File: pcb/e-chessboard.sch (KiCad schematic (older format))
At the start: 66 parts, among them J1 POWER, J2 UART, Q1 BC847, Q2 BC847, SW1 Reset, SW2 Boot, U1 ESP32-WROOM-32U, U10 MAGNET_LDR, U11 MAGNET_LDR, U12 MAGNET_LDR, U13 NCV7608, U2 AOZ1280, U3 NCV7608, U4 MAGNET_LDR, U5 MAGNET_LDR, U6 MAGNET_LDR, U7 MAGNET_LDR, U8 MAGNET_LDR, U9 MAGNET_LDR

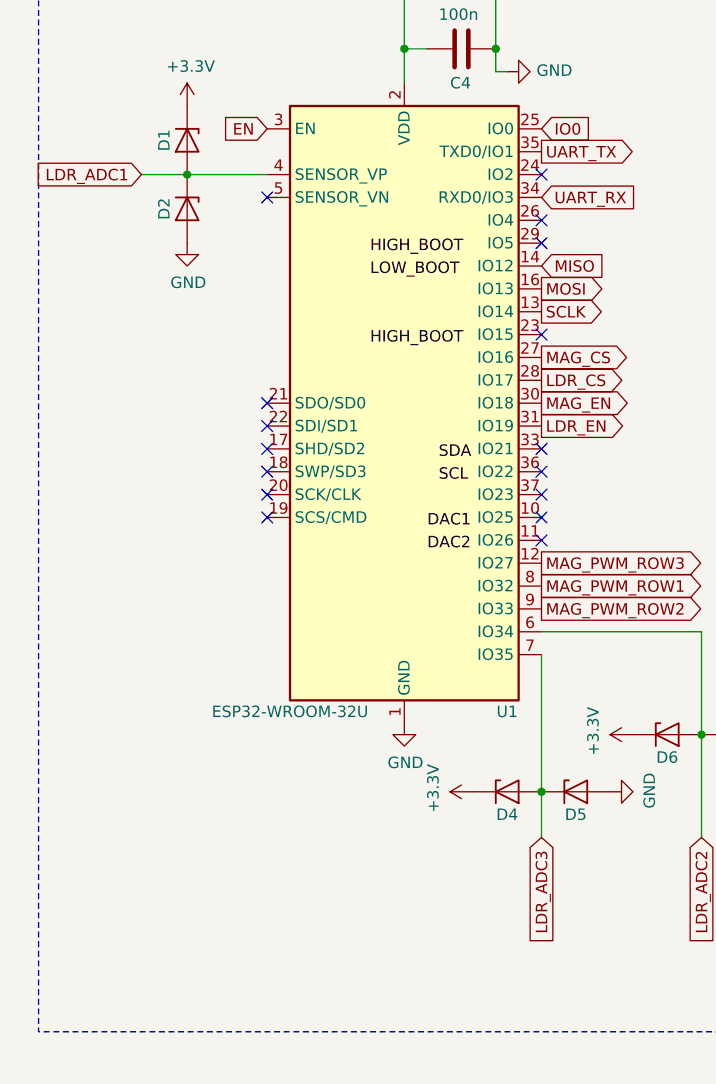
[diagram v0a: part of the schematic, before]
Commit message: fix(kicad): redesign pcb
Redesigning the pcb with the new ldr matrix.
I'm pretty sure, that's it's still not working, but for the first
prototype I will put the focus on the magnets and not the ldr. Just a
prove a concept.
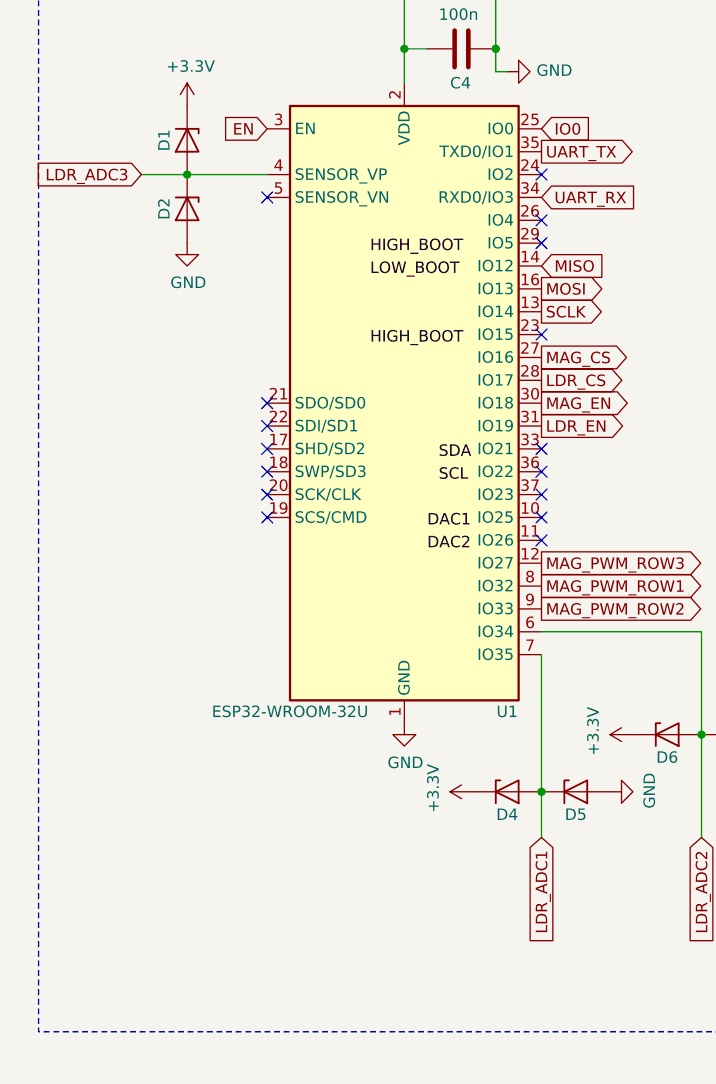
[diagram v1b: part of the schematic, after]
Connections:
- net LDR_ADC1: now also D4.2 (A), D5.1 (K), U1.7 (IO35); no longer D1.2 (A), D2.1 (K), U1.4 (SENSOR_VP)
- net LDR_ADC3: now also D1.2 (A), D2.1 (K), U1.4 (SENSOR_VP); no longer D4.2 (A), D5.1 (K), U1.7 (IO35)
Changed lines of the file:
@@
 MAG_COL_3
 $Comp
-L power:GND #PWR025
+L power:GND #PWR026
 U 1 1 5E693B2A
 P 8750 2700
-F 0 "#PWR025" H 8750 2450 50  0001 C CNN
+F 0 "#PWR026" H 8750 2450 50  0001 C CNN
 F 1 "GND" V 8755 2572 50  0000 R CNN
 F 2 "" H 8750 2700 50  0001 C CNN
@@
 Connection ~ 8750 2700
 $Comp
-L power:GND #PWR030
+L power:GND #PWR031
 U 1 1 5E693B35
 P 9600 2750
-F 0 "#PWR030" H 9600 2500 50  0001 C CNN
+F 0 "#PWR031" H 9600 2500 50  0001 C CNN
 F 1 "GND" V 9605 2622 50  0000 R CNN
 F 2 "" H 9600 2750 50  0001 C CNN
@@
 NoConn ~ 9600 2050
 $Comp
-L power:+12V #PWR027
+L power:+12V #PWR028
 U 1 1 5E693B3E
 P 8850 1850
-F 0 "#PWR027" H 8850 1700 50  0001 C CNN
+F 0 "#PWR028" H 8850 1700 50  0001 C CNN
 F 1 "+12V" V 8865 1978 50  0000 L CNN
 F 2 "" H 8850 1850 50  0001 C CNN
@@
 $EndComp
 $Comp
-L power:+12V #PWR026
+L power:+12V #PWR027
 U 1 1 5E693B44
 P 8850 1550
-F 0 "#PWR026" H 8850 1400 50  0001 C CNN
+F 0 "#PWR027" H 8850 1400 50  0001 C CNN
 F 1 "+12V" V 8865 1678 50  0000 L CNN
 F 2 "" H 8850 1550 50  0001 C CNN
@@
 $EndComp
 $Comp
-L power:+12V #PWR029
+L power:+12V #PWR030
 U 1 1 5E693B4A
 P 9600 1550
-F 0 "#PWR029" H 9600 1400 50  0001 C CNN
+F 0 "#PWR030" H 9600 1400 50  0001 C CNN
 F 1 "+12V" V 9615 1678 50  0000 L CNN
 F 2 "" H 9600 1550 50  0001 C CNN
@@
 NoConn ~ 9600 1850
 $Comp
-L power:GND #PWR028
+L power:GND #PWR029
 U 1 1 5E6A7D5E
 P 8850 2450
-F 0 "#PWR028" H 8850 2200 50  0001 C CNN
+F 0 "#PWR029" H 8850 2200 50  0001 C CNN
 F 1 "GND" V 8855 2322 50  0000 R CNN
 F 2 "" H 8850 2450 50  0001 C CNN
@@
 $EndComp
 $Comp
-L power:+12V #PWR032
+L power:+12V #PWR033
 U 1 1 5E6A7F72
 P 10150 1950
-F 0 "#PWR032" H 10150 1800 50  0001 C CNN
+F 0 "#PWR033" H 10150 1800 50  0001 C CNN
 F 1 "+12V" V 10165 2078 50  0000 L CNN
 F 2 "" H 10150 1950 50  0001 C CNN
@@
 $EndComp
 $Comp
-L power:GND #PWR031
+L power:GND #PWR032
 U 1 1 5E6A8CA5
 P 10150 1650
-F 0 "#PWR031" H 10150 1400 50  0001 C CNN
+F 0 "#PWR032" H 10150 1400 50  0001 C CNN
 F 1 "GND" H 10155 1477 50  0000 C CNN
 F 2 "" H 10150 1650 50  0001 C CNN
@@
 $EndComp
 $Comp
-L power:+3.3V #PWR023
+L power:+3.3V #PWR024
 U 1 1 5E69F100
 P 8300 2250
-F 0 "#PWR023" H 8300 2100 50  0001 C CNN
+F 0 "#PWR024" H 8300 2100 50  0001 C CNN
 F 1 "+3.3V" V 8315 2378 50  0000 L CNN
 F 2 "" H 8300 2250 50  0001 C CNN
@@
 Connection ~ 6500 6750
 $Comp
-L power:+3.3V #PWR016
+L power:+3.3V #PWR017
 U 1 1 5E89D658
 P 6500 6350
-F 0 "#PWR016" H 6500 6200 50  0001 C CNN
+F 0 "#PWR017" H 6500 6200 50  0001 C CNN
 F 1 "+3.3V" H 6550 6350 50  0000 L CNN
 F 2 "" H 6500 6350 50  0001 C CNN
@@
 $EndComp
 $Comp
-L power:GND #PWR017
+L power:GND #PWR018
 U 1 1 5E89DCA1
 P 6500 7050
-F 0 "#PWR017" H 6500 6800 50  0001 C CNN
+F 0 "#PWR018" H 6500 6800 50  0001 C CNN
 F 1 "GND" H 6650 7050 50  0000 R CNN
 F 2 "" H 6500 7050 50  0001 C CNN
@@
 $EndComp
 $Comp
-L power:+3.3V #PWR018
+L power:+3.3V #PWR019
 U 1 1 5E8B01DC
 P 6500 7550
-F 0 "#PWR018" H 6500 7400 50  0001 C CNN
+F 0 "#PWR019" H 6500 7400 50  0001 C CNN
 F 1 "+3.3V" H 6550 7600 50  0000 L CNN
 F 2 "" H 6500 7550 50  0001 C CNN
@@
 	7850 7350 7850 7250
 $Comp
-L power:GND #PWR022
+L power:GND #PWR023
 U 1 1 5E8D6B40
 P 7950 7250
-F 0 "#PWR022" H 7950 7000 50  0001 C CNN
+F 0 "#PWR023" H 7950 7000 50  0001 C CNN
 F 1 "GND" V 8000 7350 50  0000 R CNN
 F 2 "" H 7950 7250 50  0001 C CNN
@@
 $EndComp
 $Comp
-L power:+3.3V #PWR020
+L power:+3.3V #PWR021
 U 1 1 5E8F3DEC
 P 7750 8150
-F 0 "#PWR020" H 7750 8000 50  0001 C CNN
+F 0 "#PWR021" H 7750 8000 50  0001 C CNN
 F 1 "+3.3V" V 7765 8278 50  0000 L CNN
 F 2 "" H 7750 8150 50  0001 C CNN
@@
 $EndComp
 $Comp
-L power:GND #PWR019
+L power:GND #PWR020
 U 1 1 5E8FAC1F
 P 7750 8050
-F 0 "#PWR019" H 7750 7800 50  0001 C CNN
+F 0 "#PWR020" H 7750 7800 50  0001 C CNN
 F 1 "GND" V 7755 7922 50  0000 R CNN
 F 2 "" H 7750 8050 50  0001 C CNN
@@
 EN
 $Comp
-L power:GND #PWR024
+L power:GND #PWR025
 U 1 1 5E6A4B4A
 P 8300 2550
-F 0 "#PWR024" H 8300 2300 50  0001 C CNN
+F 0 "#PWR025" H 8300 2300 50  0001 C CNN
 F 1 "GND" H 8305 2377 50  0000 C CNN
 F 2 "" H 8300 2550 50  0001 C CNN
@@
 	7850 6750 7850 6650
 $Comp
-L power:GND #PWR021
+L power:GND #PWR022
 U 1 1 5EC99E9E
 P 7950 6650
-F 0 "#PWR021" H 7950 6400 50  0001 C CNN
+F 0 "#PWR022" H 7950 6400 50  0001 C CNN
 F 1 "GND" V 8000 6750 50  0000 R CNN
 F 2 "" H 7950 6650 50  0001 C CNN
@@
 MAG_ROW_3
 $Comp
-L power:+12V #PWR041
+L power:+12V #PWR042
 U 1 1 5F4E88F9
 P 14850 2000
-F 0 "#PWR041" H 14850 1850 50  0001 C CNN
+F 0 "#PWR042" H 14850 1850 50  0001 C CNN
 F 1 "+12V" V 14865 2128 50  0000 L CNN
 F 2 "" H 14850 2000 50  0001 C CNN
@@
 $EndComp
 $Comp
-L power:GND #PWR040
+L power:GND #PWR041
 U 1 1 5F4E8905
 P 14850 1700
-F 0 "#PWR040" H 14850 1450 50  0001 C CNN
+F 0 "#PWR041" H 14850 1450 50  0001 C CNN
 F 1 "GND" H 14855 1527 50  0000 C CNN
 F 2 "" H 14850 1700 50  0001 C CNN
@@
 Connection ~ 14850 2000
 $Comp
-L power:GND #PWR038
+L power:GND #PWR039
 U 1 1 5F4F6CE9
 P 13550 2500
-F 0 "#PWR038" H 13550 2250 50  0001 C CNN
+F 0 "#PWR039" H 13550 2250 50  0001 C CNN
 F 1 "GND" V 13555 2372 50  0000 R CNN
 F 2 "" H 13550 2500 50  0001 C CNN
@@
 $EndComp
 $Comp
-L power:+3.3V #PWR034
+L power:+3.3V #PWR035
 U 1 1 5F509788
 P 13000 2300
-F 0 "#PWR034" H 13000 2150 50  0001 C CNN
+F 0 "#PWR035" H 13000 2150 50  0001 C CNN
 F 1 "+3.3V" V 13015 2428 50  0000 L CNN
 F 2 "" H 13000 2300 50  0001 C CNN
@@
 $EndComp
 $Comp
-L power:GND #PWR035
+L power:GND #PWR036
 U 1 1 5F50978E
 P 13000 2600
-F 0 "#PWR035" H 13000 2350 50  0001 C CNN
+F 0 "#PWR036" H 13000 2350 50  0001 C CNN
 F 1 "GND" H 13005 2427 50  0000 C CNN
 F 2 "" H 13000 2600 50  0001 C CNN
@@
 Text GLabel 14300 2500 2    50   Input ~ 0
 LDR_EN
-Text GLabel 1050 4700 0    50   Input ~ 0
+Text GLabel 2800 7600 3    50   Input ~ 0
 LDR_ADC1
 Text GLabel 3500 7600 3    50   Input ~ 0
 LDR_ADC2
-Text GLabel 2800 7600 3    50   Input ~ 0
+Text GLabel 1050 4700 0    50   Input ~ 0
 LDR_ADC3
 $Comp
@@
 MAGNET_LDR_MATRIX
 $Comp
-L power:+3.3V #PWR0101
+L power:+3.3V #PWR016
 U 1 1 5FD145A0
 P 5800 2050
-F 0 "#PWR0101" H 5800 1900 50  0001 C CNN
+F 0 "#PWR016" H 5800 1900 50  0001 C CNN
 F 1 "+3.3V" H 5815 2223 50  0000 C CNN
 F 2 "" H 5800 2050 50  0001 C CNN
@@
 Connection ~ 5800 2050
 $Comp
-L power:PWR_FLAG #FLG0101
+L power:PWR_FLAG #FLG03
 U 1 1 5FD1593F
 P 5800 2050
-F 0 "#FLG0101" H 5800 2125 50  0001 C CNN
+F 0 "#FLG03" H 5800 2125 50  0001 C CNN
 F 1 "PWR_FLAG" V 5800 2178 50  0001 L CNN
 F 2 "" H 5800 2050 50  0001 C CNN
@@
 Wire Wire Line
 	13100 5600 13150 5600
-$Comp
-L Device:D D9
-U 1 1 5EF37B5F
-P 10950 5600
-F 0 "D9" V 10950 5750 50  0000 R CNN
-F 1 "D" V 10995 5679 50  0001 L CNN
-F 2 "Diode_SMD:D_SMA" H 10950 5600 50  0001 C CNN
-F 3 "http://www.smc-diodes.com/propdf/S1A-S1M%20N0560%20REV.B.pdf" H 10950 5600 50  0001 C CNN
-	1    10950 5600
-	-1   0    0    1
-$EndComp
-$Comp
-L Device:D D12
-U 1 1 5EF372F8
-P 11950 5600
-F 0 "D12" V 11950 5750 50  0000 R CNN
-F 1 "D" V 11995 5679 50  0001 L CNN
-F 2 "Diode_SMD:D_SMA" H 11950 5600 50  0001 C CNN
-F 3 "http://www.smc-diodes.com/propdf/S1A-S1M%20N0560%20REV.B.pdf" H 11950 5600 50  0001 C CNN
-	1    11950 5600
-	-1   0    0    1
-$EndComp
 $Comp
 L Device:D D15
@@
 LDR_ADC1
 $Comp
-L power:GND #PWR?
+L power:GND #PWR040
 U 1 1 60481099
 P 14300 1700
-F 0 "#PWR?" H 14300 1450 50  0001 C CNN
+F 0 "#PWR040" H 14300 1450 50  0001 C CNN
 F 1 "GND" V 14305 1572 50  0000 R CNN
 F 2 "" H 14300 1700 50  0001 C CNN
@@
 $EndComp
 $Comp
-L power:GND #PWR?
+L power:GND #PWR037
 U 1 1 60481590
 P 13550 1700
-F 0 "#PWR?" H 13550 1450 50  0001 C CNN
+F 0 "#PWR037" H 13550 1450 50  0001 C CNN
 F 1 "GND" V 13555 1572 50  0000 R CNN
 F 2 "" H 13550 1700 50  0001 C CNN
@@
 $EndComp
 $Comp
-L power:GND #PWR?
+L power:GND #PWR038
 U 1 1 604819E2
 P 13550 1800
-F 0 "#PWR?" H 13550 1550 50  0001 C CNN
+F 0 "#PWR038" H 13550 1550 50  0001 C CNN
 F 1 "GND" V 13555 1672 50  0000 R CNN
 F 2 "" H 13550 1800 50  0001 C CNN
@@
 $EndComp
 $Comp
-L power:+12V #PWR?
+L power:+12V #PWR034
 U 1 1 604870F3
 P 12500 8300
-F 0 "#PWR?" H 12500 8150 50  0001 C CNN
+F 0 "#PWR034" H 12500 8150 50  0001 C CNN
 F 1 "+12V" H 12515 8473 50  0000 C CNN
 F 2 "" H 12500 8300 50  0001 C CNN
@@
 Wire Wire Line
 	10350 7000 10700 7000
+$Comp
+L Device:D D12
+U 1 1 5EF372F8
+P 11950 5600
+F 0 "D12" V 11950 5750 50  0000 R CNN
+F 1 "D" V 11995 5679 50  0001 L CNN
+F 2 "Diode_SMD:D_SMA" H 11950 5600 50  0001 C CNN
+F 3 "http://www.smc-diodes.com/propdf/S1A-S1M%20N0560%20REV.B.pdf" H 11950 5600 50  0001 C CNN
+	1    11950 5600
+	-1   0    0    1
+$EndComp
+$Comp
+L Device:D D9
+U 1 1 5EF37B5F
+P 10950 5600
+F 0 "D9" V 10950 5750 50  0000 R CNN
+F 1 "D" V 10995 5679 50  0001 L CNN
+F 2 "Diode_SMD:D_SMA" H 10950 5600 50  0001 C CNN
+F 3 "http://www.smc-diodes.com/propdf/S1A-S1M%20N0560%20REV.B.pdf" H 10950 5600 50  0001 C CNN
+	1    10950 5600
+	-1   0    0    1
+$EndComp
 $EndSCHEMATC

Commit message: feat(kicad): removing ldr for simplification
Removing the ldr matrix for simplification. I had to switch to a two
layer board beacause of the price. See #3
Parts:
- removed C14: 100n, Capacitor_SMD:C_0805_2012Metric_Pad1.15x1.40mm_HandSolder, symbol Device:C
- removed C15: 100nF, Capacitor_SMD:C_0805_2012Metric_Pad1.15x1.40mm_HandSolder, symbol Device:C
- removed D1, D2, D4, D5, D6, D7: D_Zener, Diode_SMD:D_SOD-110, symbol Device:D_Zener
- removed R7, R8, R9: 300k, Resistor_SMD:R_0805_2012Metric, symbol Device:R
- removed U10, U11, U12, U4, U5, U6, U7, U8, U9: MAGNET_LDR, lib_fp:20_15_electromagnet_ldr, symbol lib:MAGNET_LDR
- removed U13: NCV7608, Package_SO:SOIC-28W_7.5x17.9mm_P1.27mm, symbol lib:NCV7608
- added L? (x9): INDUCTOR, lib_fp:20_15_electromagnet, symbol pspice:INDUCTOR
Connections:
- net MAG_COL_1: now also L?.2, L?.2, L?.2
- net MAG_COL_2: now also D15.2 (A), D16.2 (A), D17.2 (A), L?.1, L?.1, L?.1, L?.2, L?.2, L?.2
- net MAG_COL_3: now also D12.2 (A), D13.2 (A), D14.2 (A), L?.1, L?.1, L?.1, L?.2, L?.2, L?.2
- net MAG_CS: now also U1.23 (IO15); no longer U1.27 (IO16)
- net MAG_EN: now also U1.27 (IO16); no longer U1.30 (IO18)
- net MAG_ROW_1: now also L?.1; no longer D12.2 (A), D15.2 (A)
- net MAG_ROW_2: now also L?.1; no longer D13.2 (A), D16.2 (A)
- net MAG_ROW_3: now also L?.1; no longer D14.2 (A), D17.2 (A)
- net LDR_ADC1: no longer names the net of U1.7 (IO35)
- net LDR_ADC2: no longer names the net of U1.6 (IO34)
- net LDR_ADC3: no longer names the net of U1.4 (SENSOR_VP)
- net LDR_CS: no longer names the net of U1.28 (IO17)
- net LDR_EN: no longer names the net of U1.31 (IO19)
- no-connect marks 39 -> 30

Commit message: fix(kicad): fixing magnet matrix
Had some short circuits in the magnet matrix.
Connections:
- net MAG_COL_2: no longer D15.2 (A), D16.2 (A), D17.2 (A), L?.1, L?.1, L?.1
- net MAG_COL_3: no longer D12.2 (A), D13.2 (A), D14.2 (A), L?.1, L?.1, L?.1
- net MAG_ROW_1: now also D12.2 (A), D15.2 (A), L?.1, L?.1
- net MAG_ROW_2: now also D13.2 (A), D16.2 (A), L?.1, L?.1
- net MAG_ROW_3: now also D14.2 (A), D17.2 (A), L?.1, L?.1
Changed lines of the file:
@@
 Text GLabel 12300 5200 1    50   Input ~ 0
 MAG_COL_2
-Text GLabel 10500 5550 0    50   Input ~ 0
+Text GLabel 10500 5800 0    50   Input ~ 0
 MAG_ROW_1
 Wire Wire Line
@@
 	-1   0    0    1
 $EndComp
-Text GLabel 10500 6550 0    50   Input ~ 0
+Text GLabel 10500 6800 0    50   Input ~ 0
 MAG_ROW_2
 Wire Wire Line
@@
 	-1   0    0    1
 $EndComp
-Text GLabel 10500 7550 0    50   Input ~ 0
+Text GLabel 10500 7800 0    50   Input ~ 0
 MAG_ROW_3
 $Comp
@@
 	11200 5550 11150 5550
 Wire Wire Line
-	11300 5550 11700 5550
-Wire Wire Line
-	11300 6550 11700 6550
-Wire Wire Line
 	11200 7450 11200 7550
 Connection ~ 11200 7550
@@
 	11200 7550 11150 7550
 Wire Wire Line
-	11300 7550 11700 7550
-Connection ~ 11300 7550
-Wire Wire Line
 	12200 7550 12200 7450
 Connection ~ 12200 7550
@@
 Wire Wire Line
 	13300 6550 13300 5550
-Connection ~ 12300 7550
-Wire Wire Line
-	12300 7550 12700 7550
 Wire Wire Line
 	12300 5200 12300 5550
 Connection ~ 12300 5550
 Wire Wire Line
-	12300 5550 12700 5550
-Wire Wire Line
 	12300 5550 12300 6550
 Connection ~ 12300 6550
 Wire Wire Line
-	12300 6550 12700 6550
-Wire Wire Line
 	12300 6550 12300 7550
+Wire Wire Line
+	10500 6800 10500 6550
+Wire Wire Line
+	10500 5800 10500 5550
+Wire Wire Line
+	10500 7800 10500 7550
+Wire Wire Line
+	10500 7800 11500 7800
+Wire Wire Line
+	11500 7800 11500 7550
+Wire Wire Line
+	11500 7550 11700 7550
+Wire Wire Line
+	10500 6800 11500 6800
+Wire Wire Line
+	11500 6800 11500 6550
+Wire Wire Line
+	11500 6550 11700 6550
+Wire Wire Line
+	10500 5800 11500 5800
+Wire Wire Line
+	11500 5800 11500 5550
+Wire Wire Line
+	11500 5550 11700 5550
+Wire Wire Line
+	11500 5800 12500 5800
+Wire Wire Line
+	12500 5800 12500 5550
+Connection ~ 11500 5800
+Wire Wire Line
+	12500 5550 12700 5550
+Wire Wire Line
+	11500 6800 12500 6800
+Wire Wire Line
+	12500 6800 12500 6550
+Connection ~ 11500 6800
+Wire Wire Line
+	12500 6550 12700 6550
+Wire Wire Line
+	11500 7800 12500 7800
+Wire Wire Line
+	12500 7800 12500 7550
+Connection ~ 11500 7800
+Wire Wire Line
+	12500 7550 12700 7550
 $EndSCHEMATC

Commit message: feat(kicad): adding annotation
Adding annotation for the components.
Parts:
- gave numbers to parts that had none: 9
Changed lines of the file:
@@
 NoConn ~ 2800 6700
 $Comp
-L pspice:INDUCTOR L?
+L pspice:INDUCTOR L2
 U 1 1 5E76BC05
 P 10950 5450
-F 0 "L?" H 10950 5665 50  0000 C CNN
+F 0 "L2" H 10950 5665 50  0000 C CNN
 F 1 "INDUCTOR" H 10950 5574 50  0000 C CNN
 F 2 "lib_fp:20_15_electromagnet" H 10950 5450 50  0001 C CNN
@@
 $EndComp
 $Comp
-L pspice:INDUCTOR L?
+L pspice:INDUCTOR L5
 U 1 1 5E76CDCC
 P 11950 5450
-F 0 "L?" H 11950 5665 50  0000 C CNN
+F 0 "L5" H 11950 5665 50  0000 C CNN
 F 1 "INDUCTOR" H 11950 5574 50  0000 C CNN
 F 2 "lib_fp:20_15_electromagnet" H 11950 5450 50  0001 C CNN
@@
 $EndComp
 $Comp
-L pspice:INDUCTOR L?
+L pspice:INDUCTOR L8
 U 1 1 5E76D265
 P 12950 5450
-F 0 "L?" H 12950 5665 50  0000 C CNN
+F 0 "L8" H 12950 5665 50  0000 C CNN
 F 1 "INDUCTOR" H 12950 5574 50  0000 C CNN
 F 2 "lib_fp:20_15_electromagnet" H 12950 5450 50  0001 C CNN
@@
 $EndComp
 $Comp
-L pspice:INDUCTOR L?
+L pspice:INDUCTOR L3
 U 1 1 5E76D75C
 P 10950 6450
-F 0 "L?" H 10950 6665 50  0000 C CNN
+F 0 "L3" H 10950 6665 50  0000 C CNN
 F 1 "INDUCTOR" H 10950 6574 50  0000 C CNN
 F 2 "lib_fp:20_15_electromagnet" H 10950 6450 50  0001 C CNN
@@
 $EndComp
 $Comp
-L pspice:INDUCTOR L?
+L pspice:INDUCTOR L6
 U 1 1 5E76DE5D
 P 11950 6450
-F 0 "L?" H 11950 6665 50  0000 C CNN
+F 0 "L6" H 11950 6665 50  0000 C CNN
 F 1 "INDUCTOR" H 11950 6574 50  0000 C CNN
 F 2 "lib_fp:20_15_electromagnet" H 11950 6450 50  0001 C CNN
@@
 $EndComp
 $Comp
-L pspice:INDUCTOR L?
+L pspice:INDUCTOR L9
 U 1 1 5E76E38E
 P 12950 6450
-F 0 "L?" H 12950 6665 50  0000 C CNN
+F 0 "L9" H 12950 6665 50  0000 C CNN
 F 1 "INDUCTOR" H 12950 6574 50  0000 C CNN
 F 2 "lib_fp:20_15_electromagnet" H 12950 6450 50  0001 C CNN
@@
 $EndComp
 $Comp
-L pspice:INDUCTOR L?
+L pspice:INDUCTOR L4
 U 1 1 5E76E8F6
 P 10950 7450
-F 0 "L?" H 10950 7665 50  0000 C CNN
+F 0 "L4" H 10950 7665 50  0000 C CNN
 F 1 "INDUCTOR" H 10950 7574 50  0000 C CNN
 F 2 "lib_fp:20_15_electromagnet" H 10950 7450 50  0001 C CNN
@@
 $EndComp
 $Comp
-L pspice:INDUCTOR L?
+L pspice:INDUCTOR L7
 U 1 1 5E76F37D
 P 11950 7450
-F 0 "L?" H 11950 7665 50  0000 C CNN
+F 0 "L7" H 11950 7665 50  0000 C CNN
 F 1 "INDUCTOR" H 11950 7574 50  0000 C CNN
 F 2 "lib_fp:20_15_electromagnet" H 11950 7450 50  0001 C CNN
@@
 $EndComp
 $Comp
-L pspice:INDUCTOR L?
+L pspice:INDUCTOR L10
 U 1 1 5E76FF24
 P 12950 7450
-F 0 "L?" H 12950 7665 50  0000 C CNN
+F 0 "L10" H 12950 7665 50  0000 C CNN
 F 1 "INDUCTOR" H 12950 7574 50  0000 C CNN
 F 2 "lib_fp:20_15_electromagnet" H 12950 7450 50  0001 C CNN

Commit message: fix(kicad): fixing pin order of pwm
Adjusting the pin order of the pwm lines for better line laying.
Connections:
- net MAG_PWM_ROW1: now also U1.12 (IO27); no longer U1.8 (IO32)
- net MAG_PWM_ROW3: now also U1.8 (IO32); no longer U1.12 (IO27)
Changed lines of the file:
@@
 Text GLabel 9600 2150 2    50   Input ~ 0
 MAG_PWM_ROW3
-Text GLabel 2800 6500 2    50   Output ~ 0
+Text GLabel 2800 6400 2    50   Output ~ 0
 MAG_PWM_ROW1
 Text GLabel 2800 6600 2    50   Output ~ 0
 MAG_PWM_ROW2
-Text GLabel 2800 6400 2    50   Output ~ 0
+Text GLabel 2800 6500 2    50   Output ~ 0
 MAG_PWM_ROW3
 Text GLabel 9600 2450 2    50   Input ~ 0

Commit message: feat(kicad): wireing mosfet driver
Completly wirering the mosfet driver ic.
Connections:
- net MAG_EN: now also U1.11 (IO26); no longer U1.27 (IO16)
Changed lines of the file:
@@
 Text GLabel 9600 2450 2    50   Input ~ 0
 MAG_EN
-Text GLabel 2800 5500 2    50   Output ~ 0
+Text GLabel 2800 6300 2    50   Output ~ 0
 MAG_EN
 Text GLabel 8850 2150 0    50   Input ~ 0
@@
 NoConn ~ 2800 4700
 NoConn ~ 2800 4900
-NoConn ~ 2800 5000
+NoConn ~ 2800 5500
 NoConn ~ 2800 5900
 NoConn ~ 2800 6000
 NoConn ~ 2800 6100
 NoConn ~ 2800 6200
-NoConn ~ 2800 6300
+NoConn ~ 2800 5000
 Text GLabel 2800 4600 2    50   Output ~ 0
 UART_TX

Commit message: feat(kicad): adding 0R resistor for programmer safty
Adding a zero ohm resistor between the buck converter and the progrmamer
3.3v line for safty reasons.
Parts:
- added R7: 0, Resistor_SMD:R_0805_2012Metric, symbol Device:R
- renumbered D3 to D1, D16 to D10, D17 to D11, D8 to D2, D9 to D3, D10 to D4, D11 to D5, D12 to D6, D13 to D7, D14 to D8, D15 to D9
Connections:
- net +3V3: now also R7.2; no longer J2.1 (Pin_1)
- new net: J2.1 (Pin_1), R7.1
- no-connect marks 30 -> 31
